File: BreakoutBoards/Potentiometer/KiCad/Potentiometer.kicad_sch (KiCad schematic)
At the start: 2 parts, among them J1 Conn_01x03_Pin

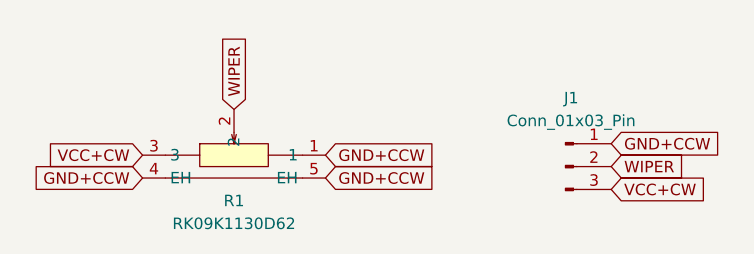
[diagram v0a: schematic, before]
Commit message: ran DRC and resolved issues
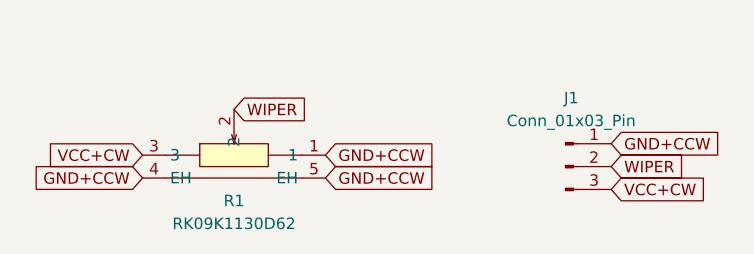
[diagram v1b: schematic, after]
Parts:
- J1: footprint clectric-diy:HDR-TH_3P-P2.54-V-M-1 -> Connector_PinHeader_2.54mm:PinHeader_1x03_P2.54mm_Vertical
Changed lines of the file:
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@@
 	(global_label "WIPER"
 		(shape input)
-		(at 69.85 104.14 90)
-		(fields_autoplaced yes)
-		(effects
-			(font
-				(size 1.27 1.27)
-			)
-			(justify left)
-		)
-		(property "Intersheetrefs" "${INTERSHEET_REFS}"
-			(at 69.85 95.4096 90)
+		(at 69.85 104.14 0)
+		(fields_autoplaced yes)
+		(effects
+			(font
+				(size 1.27 1.27)
+			)
+			(justify left)
+		)
+		(property "Intersheetrefs" "${INTERSHEET_REFS}"
+			(at 78.5804 104.14 0)
 			(effects
 				(font
@@
 			)
 		)
-		(property "Footprint" "clectric-diy:HDR-TH_3P-P2.54-V-M-1"
+		(property "Footprint" "Connector_PinHeader_2.54mm:PinHeader_1x03_P2.54mm_Vertical"
 			(at 106.68 110.49 0)
 			(effects
